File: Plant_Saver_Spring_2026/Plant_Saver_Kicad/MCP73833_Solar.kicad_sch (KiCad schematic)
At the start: 4 parts, among them U16 MCP73833-xxx-UN

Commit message: Updates to power schematic
Replaced certain selection transistors for lower Rds_on, added thermal cutoff and DW03 for battery protection, swapped in 4-channel op-amps for solar measurement, various misc. improvements.
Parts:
- C4, C5: footprint (none) -> C410C105K5R5TA7200:CAP_C410C_AX_X7R_AXIMAX_KEM
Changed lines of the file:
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@@
 			)
 		)
-		(property "Footprint" ""
+		(property "Footprint" "C410C105K5R5TA7200:CAP_C410C_AX_X7R_AXIMAX_KEM"
 			(at 150.8252 88.9 0)
 			(effects
@@
 			)
 		)
-		(property "Footprint" ""
+		(property "Footprint" "C410C105K5R5TA7200:CAP_C410C_AX_X7R_AXIMAX_KEM"
 			(at 107.6452 88.9 0)
 			(effects

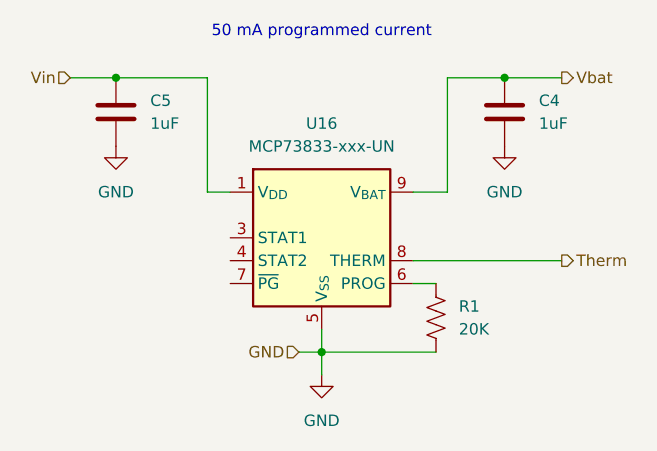
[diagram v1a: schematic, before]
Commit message: Footprint correction
Changed the DHT20 from a header pin to the recommended SIP. Also had to reannotate in order to assign footprints.
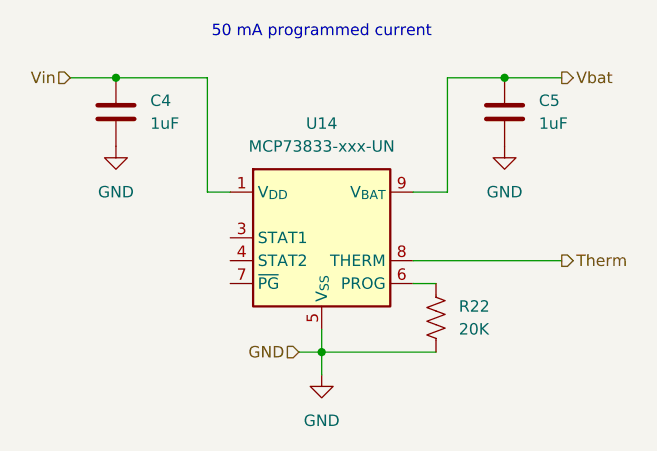
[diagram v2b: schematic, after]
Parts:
- renumbered C5 to C4, C4 to C5, R1 to R22, U16 to U14
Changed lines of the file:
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@@
 		(dnp no)
 		(fields_autoplaced yes)
-		(property "Reference" "#PWR08"
+		(property "Reference" "#PWR026"
 			(at 149.86 95.25 0)
 			(effects
@@
 			(project "Plant_Saver_Kicad"
 				(path "/7f244634-d37a-4ff0-ba36-8027330ab1bd/c1b5c94f-5fb5-4e2b-895b-5d171c372d7d/88ce505a-5a66-4cd3-8edd-ee3f7ea8c6c0"
-					(reference "#PWR08")
+					(reference "#PWR026")
 					(unit 1)
 				)
@@
 		(dnp no)
 		(fields_autoplaced yes)
-		(property "Reference" "U16"
+		(property "Reference" "U14"
 			(at 129.54 86.36 0)
 			(effects
@@
 			(project ""
 				(path "/7f244634-d37a-4ff0-ba36-8027330ab1bd/c1b5c94f-5fb5-4e2b-895b-5d171c372d7d/88ce505a-5a66-4cd3-8edd-ee3f7ea8c6c0"
-					(reference "U16")
+					(reference "U14")
 					(unit 1)
 				)
@@
 		(dnp no)
 		(fields_autoplaced yes)
-		(property "Reference" "C4"
+		(property "Reference" "C5"
 			(at 153.67 83.8199 0)
 			(effects
@@
 			(project "Plant_Saver_Kicad"
 				(path "/7f244634-d37a-4ff0-ba36-8027330ab1bd/c1b5c94f-5fb5-4e2b-895b-5d171c372d7d/88ce505a-5a66-4cd3-8edd-ee3f7ea8c6c0"
-					(reference "C4")
+					(reference "C5")
 					(unit 1)
 				)
@@
 		(dnp no)
 		(fields_autoplaced yes)
-		(property "Reference" "#PWR09"
+		(property "Reference" "#PWR024"
 			(at 106.68 95.25 0)
 			(effects
@@
 			(project "Plant_Saver_Kicad"
 				(path "/7f244634-d37a-4ff0-ba36-8027330ab1bd/c1b5c94f-5fb5-4e2b-895b-5d171c372d7d/88ce505a-5a66-4cd3-8edd-ee3f7ea8c6c0"
-					(reference "#PWR09")
+					(reference "#PWR024")
 					(unit 1)
 				)
@@
 		(dnp no)
 		(fields_autoplaced yes)
-		(property "Reference" "R1"
+		(property "Reference" "R22"
 			(at 144.78 106.6799 0)
 			(effects
@@
 			(project "Plant_Saver_Kicad"
 				(path "/7f244634-d37a-4ff0-ba36-8027330ab1bd/c1b5c94f-5fb5-4e2b-895b-5d171c372d7d/88ce505a-5a66-4cd3-8edd-ee3f7ea8c6c0"
-					(reference "R1")
+					(reference "R22")
 					(unit 1)
 				)
@@
 		(dnp no)
 		(fields_autoplaced yes)
-		(property "Reference" "C5"
+		(property "Reference" "C4"
 			(at 110.49 83.8199 0)
 			(effects
@@
 			(project "Plant_Saver_Kicad"
 				(path "/7f244634-d37a-4ff0-ba36-8027330ab1bd/c1b5c94f-5fb5-4e2b-895b-5d171c372d7d/88ce505a-5a66-4cd3-8edd-ee3f7ea8c6c0"
-					(reference "C5")
+					(reference "C4")
 					(unit 1)
 				)
@@
 		(dnp no)
 		(fields_autoplaced yes)
-		(property "Reference" "#PWR07"
+		(property "Reference" "#PWR025"
 			(at 129.54 120.65 0)
 			(effects
@@
 			(project ""
 				(path "/7f244634-d37a-4ff0-ba36-8027330ab1bd/c1b5c94f-5fb5-4e2b-895b-5d171c372d7d/88ce505a-5a66-4cd3-8edd-ee3f7ea8c6c0"
-					(reference "#PWR07")
-					(unit 1)
-				)
+					(reference "#PWR025")
+					(unit 1)
+				)

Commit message: Started PCB
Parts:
- renumbered C4 to C11, C5 to C12, R22 to R24, U14 to U13
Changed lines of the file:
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@@
 		(dnp no)
 		(fields_autoplaced yes)
-		(property "Reference" "#PWR026"
+		(property "Reference" "#PWR029"
 			(at 149.86 95.25 0)
 			(effects
@@
 			(project "Plant_Saver_Kicad"
 				(path "/7f244634-d37a-4ff0-ba36-8027330ab1bd/c1b5c94f-5fb5-4e2b-895b-5d171c372d7d/88ce505a-5a66-4cd3-8edd-ee3f7ea8c6c0"
-					(reference "#PWR026")
+					(reference "#PWR029")
 					(unit 1)
 				)
@@
 		(dnp no)
 		(fields_autoplaced yes)
-		(property "Reference" "U14"
+		(property "Reference" "U13"
 			(at 129.54 86.36 0)
 			(effects
@@
 			(project ""
 				(path "/7f244634-d37a-4ff0-ba36-8027330ab1bd/c1b5c94f-5fb5-4e2b-895b-5d171c372d7d/88ce505a-5a66-4cd3-8edd-ee3f7ea8c6c0"
-					(reference "U14")
+					(reference "U13")
 					(unit 1)
 				)
@@
 		(dnp no)
 		(fields_autoplaced yes)
-		(property "Reference" "C5"
+		(property "Reference" "C12"
 			(at 153.67 83.8199 0)
 			(effects
@@
 			(project "Plant_Saver_Kicad"
 				(path "/7f244634-d37a-4ff0-ba36-8027330ab1bd/c1b5c94f-5fb5-4e2b-895b-5d171c372d7d/88ce505a-5a66-4cd3-8edd-ee3f7ea8c6c0"
-					(reference "C5")
+					(reference "C12")
 					(unit 1)
 				)
@@
 		(dnp no)
 		(fields_autoplaced yes)
-		(property "Reference" "#PWR024"
+		(property "Reference" "#PWR027"
 			(at 106.68 95.25 0)
 			(effects
@@
 			(project "Plant_Saver_Kicad"
 				(path "/7f244634-d37a-4ff0-ba36-8027330ab1bd/c1b5c94f-5fb5-4e2b-895b-5d171c372d7d/88ce505a-5a66-4cd3-8edd-ee3f7ea8c6c0"
-					(reference "#PWR024")
+					(reference "#PWR027")
 					(unit 1)
 				)
@@
 		(dnp no)
 		(fields_autoplaced yes)
-		(property "Reference" "R22"
+		(property "Reference" "R24"
 			(at 144.78 106.6799 0)
 			(effects
@@
 			(project "Plant_Saver_Kicad"
 				(path "/7f244634-d37a-4ff0-ba36-8027330ab1bd/c1b5c94f-5fb5-4e2b-895b-5d171c372d7d/88ce505a-5a66-4cd3-8edd-ee3f7ea8c6c0"
-					(reference "R22")
+					(reference "R24")
 					(unit 1)
 				)
@@
 		(dnp no)
 		(fields_autoplaced yes)
-		(property "Reference" "C4"
+		(property "Reference" "C11"
 			(at 110.49 83.8199 0)
 			(effects
@@
 			(project "Plant_Saver_Kicad"
 				(path "/7f244634-d37a-4ff0-ba36-8027330ab1bd/c1b5c94f-5fb5-4e2b-895b-5d171c372d7d/88ce505a-5a66-4cd3-8edd-ee3f7ea8c6c0"
-					(reference "C4")
+					(reference "C11")
 					(unit 1)
 				)
@@
 		(dnp no)
 		(fields_autoplaced yes)
-		(property "Reference" "#PWR025"
+		(property "Reference" "#PWR028"
 			(at 129.54 120.65 0)
 			(effects
@@
 			(project ""
 				(path "/7f244634-d37a-4ff0-ba36-8027330ab1bd/c1b5c94f-5fb5-4e2b-895b-5d171c372d7d/88ce505a-5a66-4cd3-8edd-ee3f7ea8c6c0"
-					(reference "#PWR025")
-					(unit 1)
-				)
+					(reference "#PWR028")
+					(unit 1)
+				)

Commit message: Refined PCB layout
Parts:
- C11, C12: footprint C410C105K5R5TA7200:CAP_C410C_AX_X7R_AXIMAX_KEM -> Capacitor_SMD:C_1206_3216Metric_Pad1.33x1.80mm_HandSolder
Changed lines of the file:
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@@
 			)
 		)
-		(property "Footprint" "C410C105K5R5TA7200:CAP_C410C_AX_X7R_AXIMAX_KEM"
+		(property "Footprint" "Capacitor_SMD:C_1206_3216Metric_Pad1.33x1.80mm_HandSolder"
 			(at 150.8252 88.9 0)
 			(effects
@@
 			)
 		)
-		(property "Footprint" "C410C105K5R5TA7200:CAP_C410C_AX_X7R_AXIMAX_KEM"
+		(property "Footprint" "Capacitor_SMD:C_1206_3216Metric_Pad1.33x1.80mm_HandSolder"
 			(at 107.6452 88.9 0)
 			(effects

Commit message: PCB Pre-Check complete
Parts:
- renumbered R24 to R26
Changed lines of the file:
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@@
 		(dnp no)
 		(fields_autoplaced yes)
-		(property "Reference" "R24"
+		(property "Reference" "R26"
 			(at 144.78 106.6799 0)
 			(effects
@@
 			(project "Plant_Saver_Kicad"
 				(path "/7f244634-d37a-4ff0-ba36-8027330ab1bd/c1b5c94f-5fb5-4e2b-895b-5d171c372d7d/88ce505a-5a66-4cd3-8edd-ee3f7ea8c6c0"
-					(reference "R24")
+					(reference "R26")
 					(unit 1)
 				)
